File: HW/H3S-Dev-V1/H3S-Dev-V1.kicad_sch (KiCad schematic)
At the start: 45 parts, among them J1 USB_C_Receptacle_USB2.0_16P, J2 Conn_01x02_Socket, J3 Conn_Coaxial, J4 Conn_01x04, J5 Conn_01x04, Q1 DMP3099L, SW1 SW_Push, U1 Ai-Thinker-Ra-01, U2 LTC4054ES5-4.2, U3 USBLC6-2SC6, U4 ESP32-S3-WROOM-1, U5 SY8089AAAC, U6 L96-M33

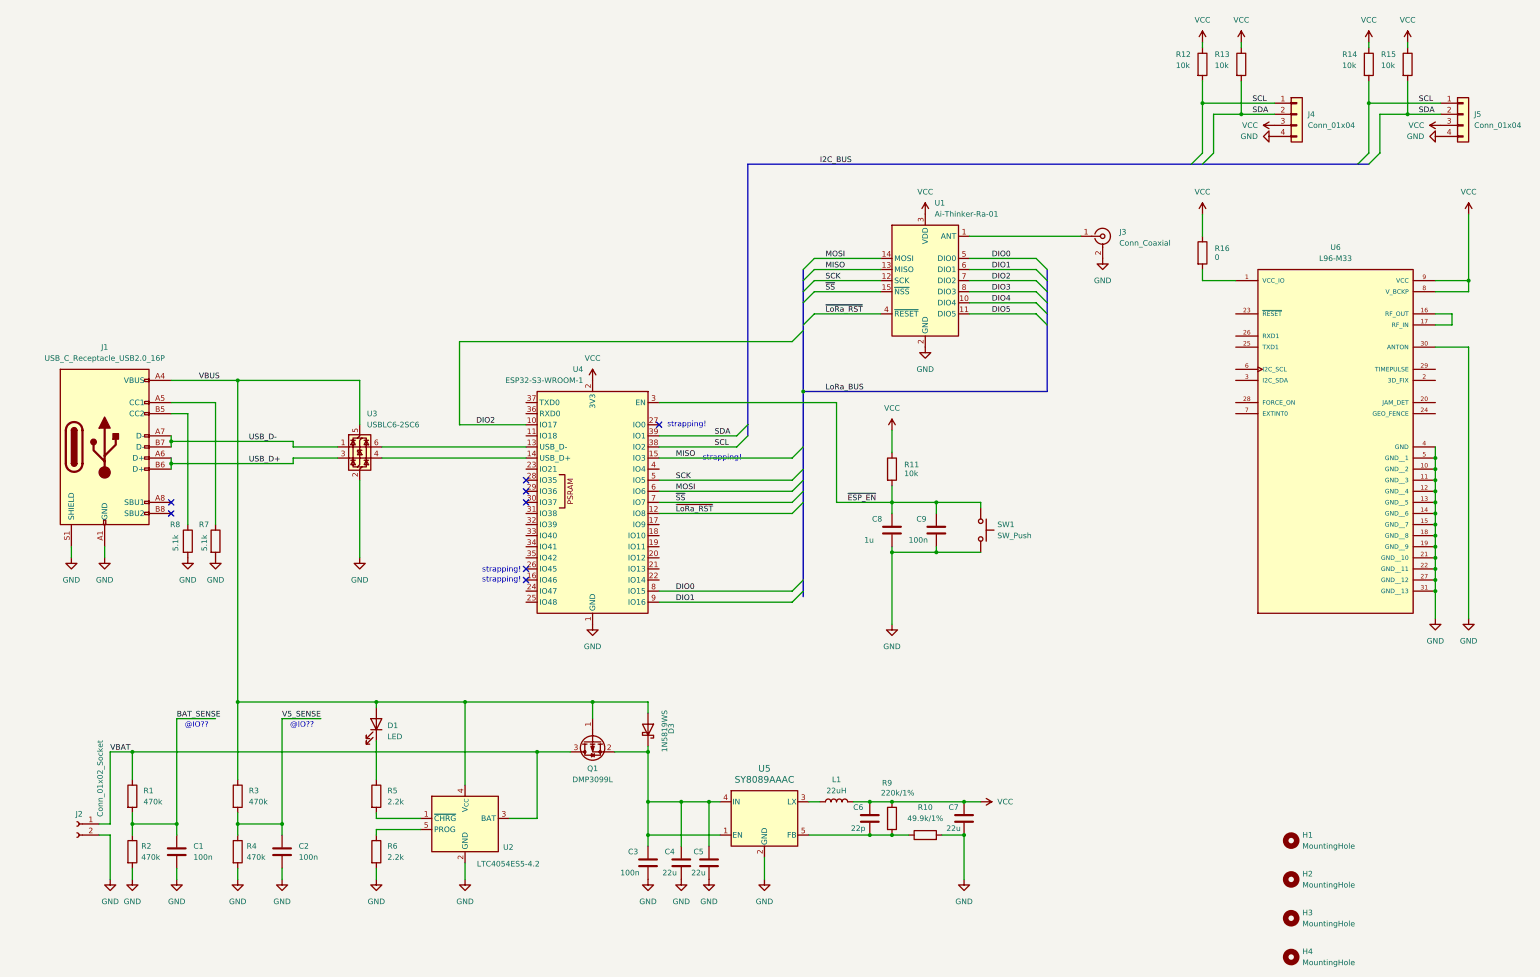
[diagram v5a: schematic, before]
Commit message: RA-01SH-P LoRa module added
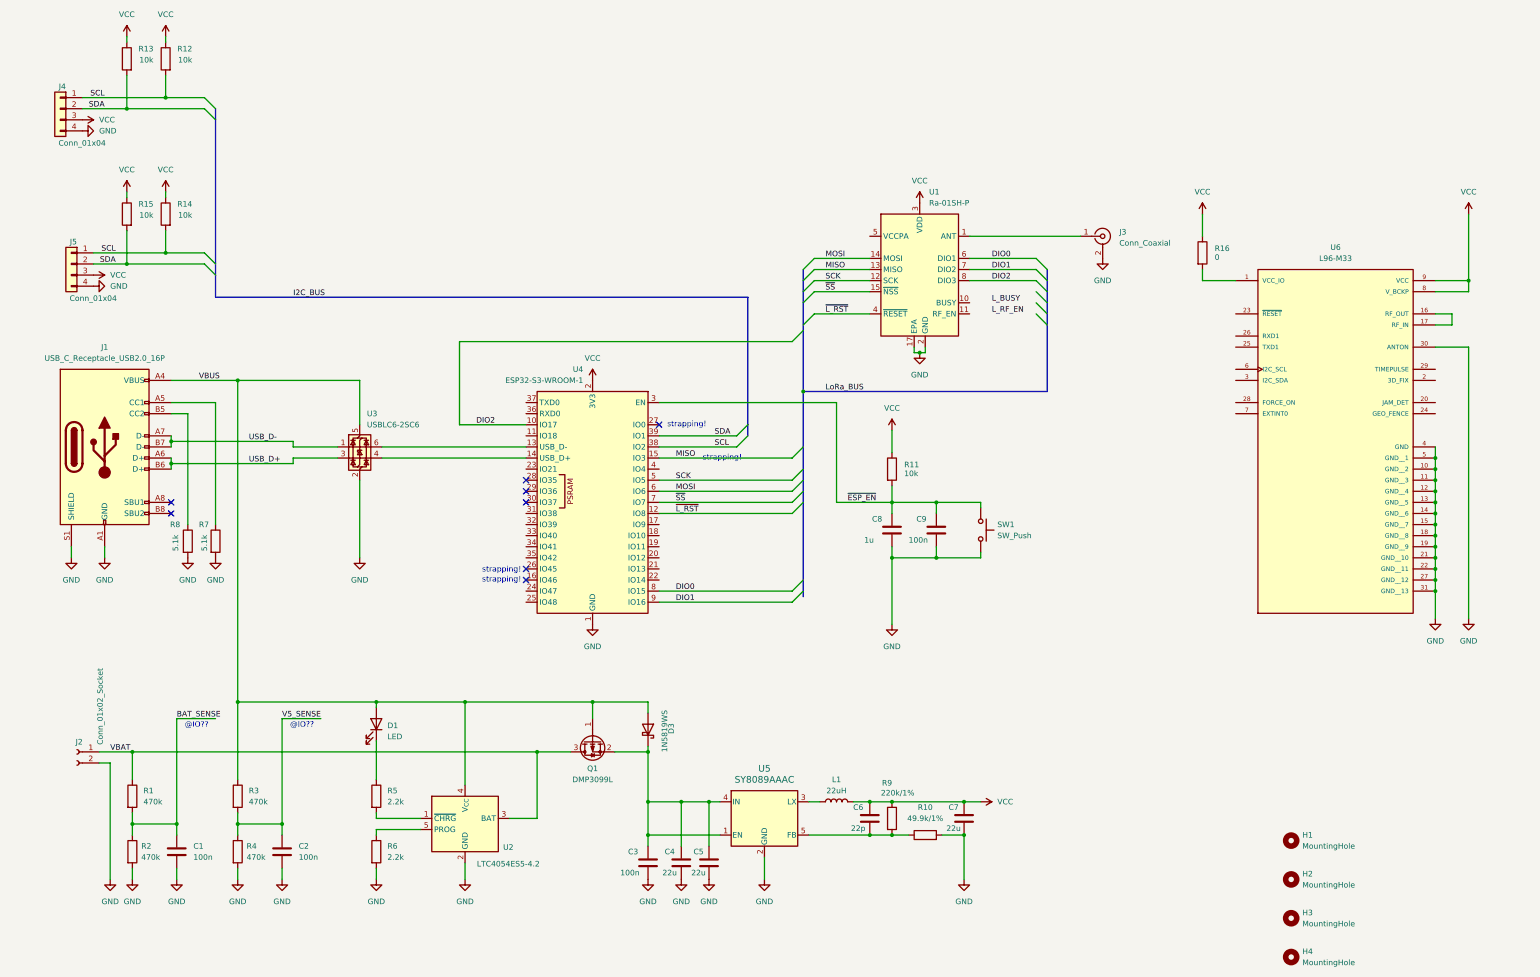
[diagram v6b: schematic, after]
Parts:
- removed U1: Ai-Thinker-Ra-01, RF_Module:Ai-Thinker-Ra-01-LoRa, symbol RF_Module:Ai-Thinker-Ra-01
- added U1: Ra-01SH-P, H3S-Dev:Ra-01SH-P, symbol H3S-Dev:Ra-01SH-P
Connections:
- net DIO0: now also U1.6 (DIO1)
- net DIO1: now also U1.7 (DIO2)
- net DIO2: now also U1.8 (DIO3)
- net GND: now also U1.16 (GND), U1.17 (EPA), U1.2 (GND), U1.9 (GND)
- net MISO: now also U1.13 (MISO)
- net MOSI: now also U1.14 (MOSI)
- net SCK: now also U1.12 (SCK)
- net VCC: now also U1.3 (VDD)
- net ~{SS}: now also U1.15 (~{NSS})
- net at J3.1 (In): now also U1.1 (ANT)
- net ~{LoRa_RST} renamed ~{L_RST}
- net ~{L_RST}: now also U1.4 (~{RESET})
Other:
- moved on the sheet: J2, J4, J5, R12, R13, R14, R15

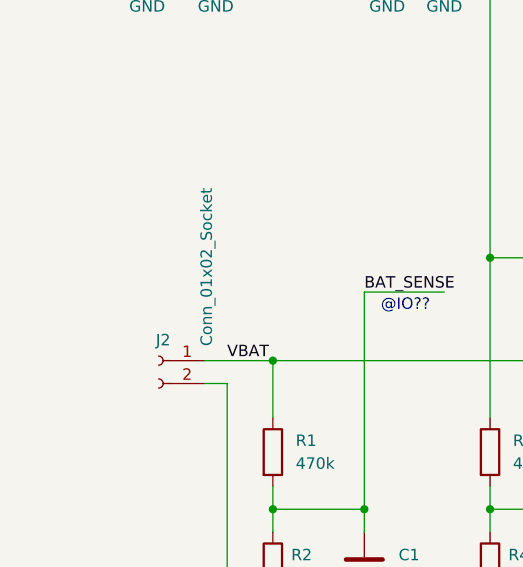
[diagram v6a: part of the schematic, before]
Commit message: J2 updated
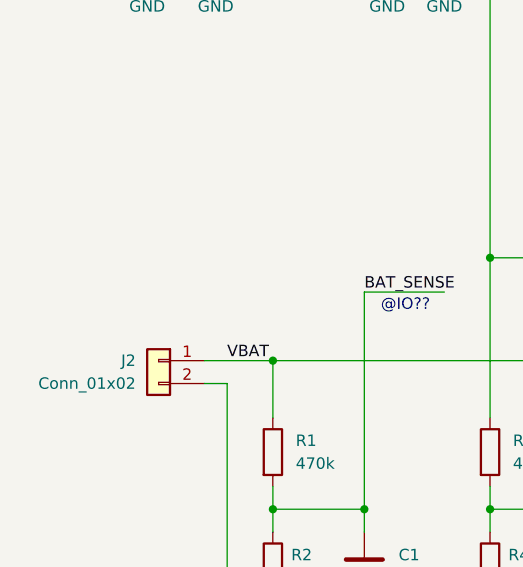
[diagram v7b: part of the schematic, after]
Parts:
- removed J2: Conn_01x02_Socket, Connector_JST:JST_PH_B2B-PH-K_1x02_P2.00mm_Vertical, symbol Connector:Conn_01x02_Socket
- added J2: Conn_01x02, Connector_JST:JST_PH_B2B-PH-K_1x02_P2.00mm_Vertical, symbol Connector_Generic:Conn_01x02
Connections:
- net GND: now also J2.2 (Pin_2)
- net VBAT: now also J2.1 (Pin_1)
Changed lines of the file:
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@@
+	)
+	(symbol
+		(lib_id "Connector_Generic:Conn_01x02")
+		(at 46.99 196.85 0)
+		(mirror y)
+		(unit 1)
+		(exclude_from_sim no)
+		(in_bom yes)
+		(on_board yes)
+		(dnp no)
+		(property "Reference" "J2"
+			(at 44.45 196.8499 0)
+			(effects
+				(font
+					(size 1.27 1.27)
+				)
+				(justify left)
+			)
+		)
+		(property "Value" "Conn_01x02"
+			(at 44.45 199.3899 0)
+			(effects
+				(font
+					(size 1.27 1.27)
+				)
+				(justify left)
+			)
+		)
+		(property "Footprint" "Connector_JST:JST_PH_B2B-PH-K_1x02_P2.00mm_Vertical"
+			(at 46.99 196.85 0)
+			(effects
+				(font
+					(size 1.27 1.27)
+				)
+				(hide yes)
+			)
+		)
+		(property "Datasheet" "~"
+			(at 46.99 196.85 0)
+			(effects
+				(font
+					(size 1.27 1.27)
+				)
+				(hide yes)
+			)
+		)
+		(property "Description" "Generic connector, single row, 01x02, script generated (kicad-library-utils/schlib/autogen/connector/)"
+			(at 46.99 196.85 0)
+			(effects
+				(font
+					(size 1.27 1.27)
+				)
+				(hide yes)
+			)
+		)
+		(pin "2"
+		)
+		(pin "1"
+		)
+		(instances
+			(project ""
+				(path "/bea38324-05bc-47f3-9040-a69798280d79"
+					(reference "J2")
+					(unit 1)
+				)
+			)
+		)
 	)
 	(symbol
@@
 					(unit 1)
 				)
-			)
-		)
-	)
-	(symbol
-		(lib_id "Connector:Conn_01x02_Socket")
-		(at 46.99 196.85 0)
-		(mirror y)
-		(unit 1)
-		(exclude_from_sim no)
-		(in_bom yes)
-		(on_board yes)
-		(dnp no)
-		(property "Reference" "J2"
-			(at 47.498 194.564 0)
-			(effects
-				(font
-					(size 1.27 1.27)
-				)
-			)
-		)
-		(property "Value" "Conn_01x02_Socket"
-			(at 52.324 186.436 90)
-			(effects
-				(font
-					(size 1.27 1.27)
-				)
-			)
-		)
-		(property "Footprint" "Connector_JST:JST_PH_B2B-PH-K_1x02_P2.00mm_Vertical"
-			(at 46.99 196.85 0)
-			(effects
-				(font
-					(size 1.27 1.27)
-				)
-				(hide yes)
-			)
-		)
-		(property "Datasheet" "~"
-			(at 46.99 196.85 0)
-			(effects
-				(font
-					(size 1.27 1.27)
-				)
-				(hide yes)
-			)
-		)
-		(property "Description" "Generic connector, single row, 01x02, script generated"
-			(at 46.99 196.85 0)
-			(effects
-				(font
-					(size 1.27 1.27)
-				)
-				(hide yes)
-			)
-		)
-		(pin "2"
-		)
-		(pin "1"
-		)
-		(instances
-			(project "S3"
-				(path "/bea38324-05bc-47f3-9040-a69798280d79"
-					(reference "J2")
-					(unit 1)
-				)

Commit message: LoRa updates
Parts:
- added C10, C11: NA, Capacitor_SMD:C_0603_1608Metric, symbol Device:C
- added R17, R18, R19: 0, Resistor_SMD:R_0603_1608Metric, symbol Device:R
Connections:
- net BAT_SENSE: now also U4.31 (IO38)
- net GND: now also C10.2, C11.2
- net L_BUSY: now also U1.10 (BUSY), U4.21 (IO13)
- net L_RF_EN: now also U4.22 (IO14), R17.2
- net V5_SENSE: now also U4.32 (IO39)
- net VCC: now also R19.1
- net at J3.1 (In): now also C11.1, R18.2; no longer U1.1 (ANT)
- net at U1.11 (RF_EN): now also R17.1
- net at U1.5 (VCCPA): now also R19.2
- new net: C10.1, R18.1, U1.1 (ANT)
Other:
- note added: "@IO38"
- note added: "@IO39"
- note removed: "@IO??"
- moved on the sheet: J3
